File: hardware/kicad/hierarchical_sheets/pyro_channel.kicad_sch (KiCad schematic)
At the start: 22 parts, among them J2 282834-2, J3 282834-4, U2 ZXCT1110W5-7, U3 SI9926CDY

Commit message: test
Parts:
- C3: value DNP -> 100n
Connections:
- net VBAT: now also J2.2 (Pin_2); no longer J2.1 (Pin_1)
- net at R1.1, R3.1, U2.4 (Vs+): now also J2.1 (Pin_1); no longer J2.2 (Pin_2)
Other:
- moved on the sheet: J2
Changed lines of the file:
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@@
     )
   )
-  (symbol (lib_id "Connector:Screw_Terminal_01x02") (at 37.465 82.55 90) (unit 1)
+  (symbol (lib_id "Connector:Screw_Terminal_01x02") (at 40.005 82.55 270) (mirror x) (unit 1)
     (in_bom yes) (on_board yes) (dnp no)
-    (property "Reference" "J2" (at 29.845 77.47 90)
+    (property "Reference" "J2" (at 43.18 77.47 90)
       (effects (font (size 1.27 1.27)) (justify right))
     )
-    (property "Value" "282834-2" (at 29.845 79.375 90)
+    (property "Value" "282834-2" (at 43.18 79.375 90)
       (effects (font (size 1.27 1.27)) (justify right))
     )
-    (property "Footprint" "TerminalBlock_TE-Connectivity:TerminalBlock_TE_282834-2_1x02_P2.54mm_Horizontal" (at 37.465 82.55 0)
+    (property "Footprint" "TerminalBlock_TE-Connectivity:TerminalBlock_TE_282834-2_1x02_P2.54mm_Horizontal" (at 40.005 82.55 0)
       (effects (font (size 1.27 1.27)) hide)
     )
-    (property "Datasheet" "https://www.te.com/usa-en/product-282834-2.datasheet.pdf" (at 37.465 82.55 0)
+    (property "Datasheet" "https://www.te.com/usa-en/product-282834-2.datasheet.pdf" (at 40.005 82.55 0)
       (effects (font (size 1.27 1.27)) hide)
     )
-    (property "Digikey" "https://www.digikey.com/en/products/detail/te-connectivity-amp-connectors/282834-2/1150135" (at 37.465 82.55 90)
+    (property "Digikey" "https://www.digikey.com/en/products/detail/te-connectivity-amp-connectors/282834-2/1150135" (at 40.005 82.55 90)
       (effects (font (size 1.27 1.27)) hide)
     )
@@
       (effects (font (size 1.27 1.27)) (justify left))
     )
-    (property "Value" "DNP" (at 94.615 114.2937 0)
+    (property "Value" "100n" (at 94.615 114.2937 0)
       (effects (font (size 1.27 1.27)) (justify left))
     )

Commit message: power routing
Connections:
- net VBAT: now also J2.1 (Pin_1); no longer J2.2 (Pin_2)
- net VBAT_SWITCHED: now reaches R1.1, R3.1, U2.4 (Vs+)
- net VBAT_SWITCHED: now also J2.2 (Pin_2); no longer J2.1 (Pin_1)
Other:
- moved on the sheet: J2
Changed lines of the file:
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@@
     (effects (font (size 1 1)) (justify left bottom))
+  )
+  (label "VBAT_SWITCHED" (at 50.165 88.265 0) (fields_autoplaced)
+    (effects (font (size 1.27 1.27)) (justify left bottom))
   )
   (label "PYRO_SUPPLY_MONITORED." (at 114.3 88.265 180) (fields_autoplaced)
@@
     )
   )
-  (symbol (lib_id "Connector:Screw_Terminal_01x02") (at 40.005 82.55 270) (mirror x) (unit 1)
-    (in_bom yes) (on_board yes) (dnp no)
-    (property "Reference" "J2" (at 43.18 77.47 90)
+  (symbol (lib_id "Connector:Screw_Terminal_01x02") (at 37.465 82.55 90) (unit 1)
+    (in_bom yes) (on_board yes) (dnp no)
+    (property "Reference" "J2" (at 34.29 77.47 90)
       (effects (font (size 1.27 1.27)) (justify right))
     )
-    (property "Value" "282834-2" (at 43.18 79.375 90)
+    (property "Value" "282834-2" (at 34.29 79.375 90)
       (effects (font (size 1.27 1.27)) (justify right))
     )
-    (property "Footprint" "TerminalBlock_TE-Connectivity:TerminalBlock_TE_282834-2_1x02_P2.54mm_Horizontal" (at 40.005 82.55 0)
-      (effects (font (size 1.27 1.27)) hide)
-    )
-    (property "Datasheet" "https://www.te.com/usa-en/product-282834-2.datasheet.pdf" (at 40.005 82.55 0)
-      (effects (font (size 1.27 1.27)) hide)
-    )
-    (property "Digikey" "https://www.digikey.com/en/products/detail/te-connectivity-amp-connectors/282834-2/1150135" (at 40.005 82.55 90)
-      (effects (font (size 1.27 1.27)) hide)
-    )
+    (property "Footprint" "TerminalBlock_TE-Connectivity:TerminalBlock_TE_282834-2_1x02_P2.54mm_Horizontal" (at 37.465 82.55 0)
+      (effects (font (size 1.27 1.27)) hide)
+    )
+    (property "Datasheet" "https://www.te.com/usa-en/product-282834-2.datasheet.pdf" (at 37.465 82.55 0)
+      (effects (font (size 1.27 1.27)) hide)
+    )
+    (property "Digikey" "https://www.digikey.com/en/products/detail/te-connectivity-amp-connectors/282834-2/1150135" (at 37.465 82.55 90)
+      (effects (font (size 1.27 1.27)) hide)
+    )

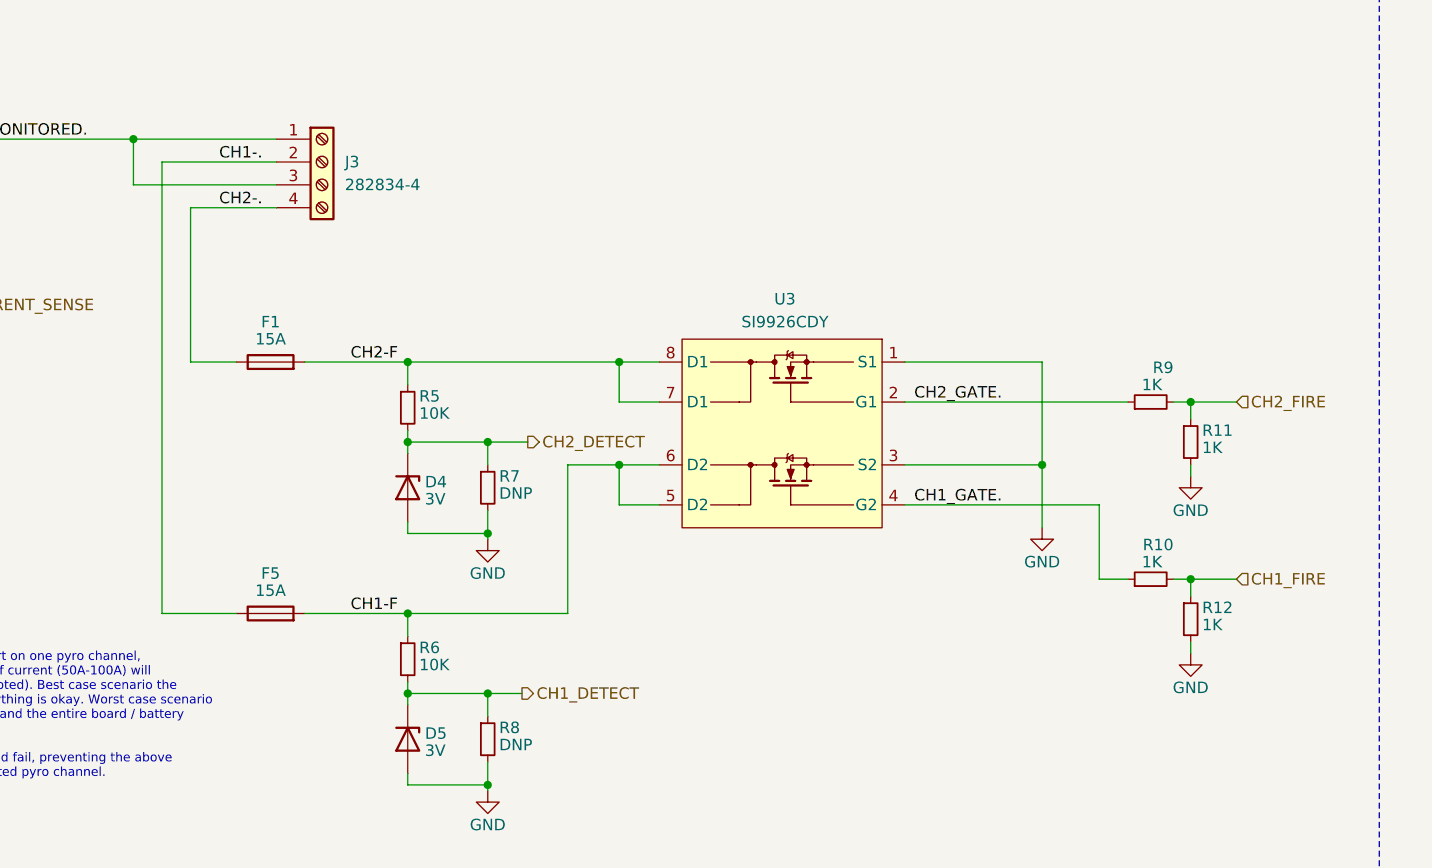
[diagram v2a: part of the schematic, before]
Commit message: redoing the beautiful traces
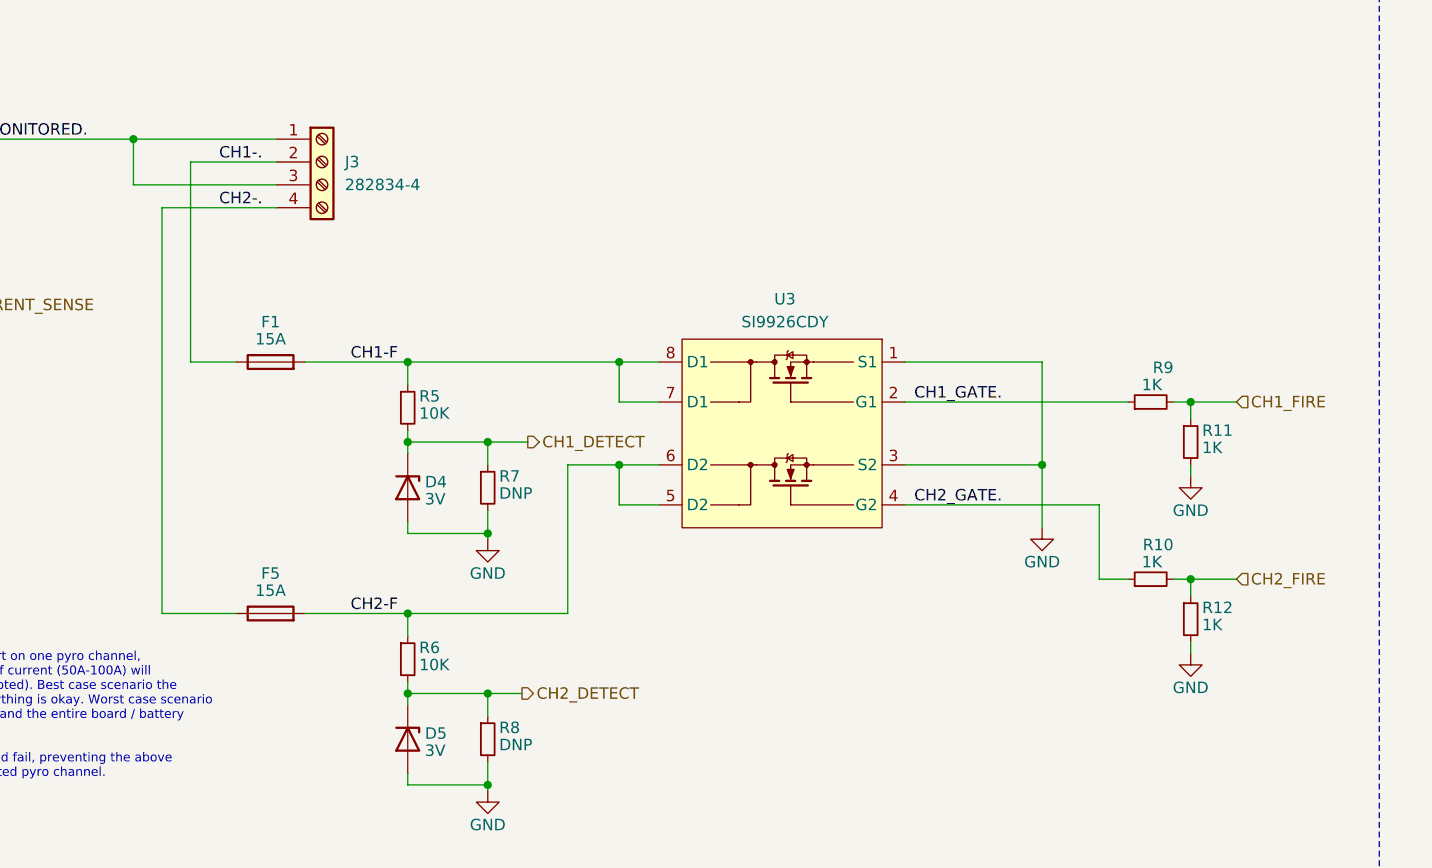
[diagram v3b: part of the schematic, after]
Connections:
- net CH1-.: now also F1.1; no longer F5.1
- net CH1-F: now also F1.2, R5.1, U3.7 (D1), U3.8 (D1); no longer F5.2, R6.1, U3.5 (D2), U3.6 (D2)
- net CH1_DETECT: now also D4.3 (K), R5.2, R7.1; no longer D5.3 (K), R6.2, R8.1
- net CH1_FIRE: now also R11.1, R9.2; no longer R10.2, R12.1
- net CH1_GATE.: now also R9.1, U3.2 (G1); no longer R10.1, U3.4 (G2)
- net CH2-.: now also F5.1; no longer F1.1
- net CH2-F: now also F5.2, R6.1, U3.5 (D2), U3.6 (D2); no longer F1.2, R5.1, U3.7 (D1), U3.8 (D1)
- net CH2_DETECT: now also D5.3 (K), R6.2, R8.1; no longer D4.3 (K), R5.2, R7.1
- net CH2_FIRE: now also R10.2, R12.1; no longer R11.1, R9.2
- net CH2_GATE.: now also R10.1, U3.4 (G2); no longer R9.1, U3.2 (G1)
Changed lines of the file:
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@@
+    (stroke (width 0) (type default))
+  )
+  (wire (pts (xy 125.73 90.805) (xy 125.73 113.03))
     (stroke (width 0) (type default))
   )
@@
     (stroke (width 0) (type default))
   )
-  (wire (pts (xy 122.555 90.805) (xy 122.555 140.97))
-    (stroke (width 0) (type default))
-  )
   (wire (pts (xy 236.855 124.46) (xy 236.855 125.73))
     (stroke (width 0) (type default))
   )
-  (wire (pts (xy 125.73 95.885) (xy 125.73 113.03))
-    (stroke (width 0) (type default))
-  )
-  (wire (pts (xy 125.73 95.885) (xy 135.255 95.885))
-    (stroke (width 0) (type default))
-  )
   (wire (pts (xy 37.465 88.265) (xy 37.465 87.63))
     (stroke (width 0) (type default))
@@
     (stroke (width 0) (type default))
   )
+  (wire (pts (xy 122.555 140.97) (xy 122.555 95.885))
+    (stroke (width 0) (type default))
+  )
   (wire (pts (xy 81.915 119.38) (xy 92.71 119.38))
     (stroke (width 0) (type default))
@@
   )
   (wire (pts (xy 149.86 148.59) (xy 149.86 149.86))
+    (stroke (width 0) (type default))
+  )
+  (wire (pts (xy 125.73 90.805) (xy 135.255 90.805))
     (stroke (width 0) (type default))
   )
@@
     (stroke (width 0) (type default))
   )
+  (wire (pts (xy 122.555 95.885) (xy 135.255 95.885))
+    (stroke (width 0) (type default))
+  )
   (polyline (pts (xy 257.81 72.39) (xy 257.81 169.545))
     (stroke (width 0) (type dash))
   )
   (wire (pts (xy 158.75 160.02) (xy 158.75 160.655))
-    (stroke (width 0) (type default))
-  )
-  (wire (pts (xy 122.555 90.805) (xy 135.255 90.805))
     (stroke (width 0) (type default))
   )
@@
     (effects (font (size 1.27 1.27)) (justify right bottom))
   )
+  (label "CH1-." (at 128.905 90.805 0) (fields_autoplaced)
+    (effects (font (size 1.27 1.27)) (justify left bottom))
+  )
+  (label "CH2-F" (at 143.51 140.97 0) (fields_autoplaced)
+    (effects (font (size 1.27 1.27)) (justify left bottom))
+  )
+  (label "CH2_GATE." (at 215.9 128.905 180) (fields_autoplaced)
+    (effects (font (size 1.27 1.27)) (justify right bottom))
+  )
+  (label "CH1_GATE." (at 215.9 117.475 180) (fields_autoplaced)
+    (effects (font (size 1.27 1.27)) (justify right bottom))
+  )
   (label "CH2-." (at 128.905 95.885 0) (fields_autoplaced)
     (effects (font (size 1.27 1.27)) (justify left bottom))
   )
-  (label "CH1-F" (at 143.51 140.97 0) (fields_autoplaced)
-    (effects (font (size 1.27 1.27)) (justify left bottom))
-  )
-  (label "CH1_GATE." (at 215.9 128.905 180) (fields_autoplaced)
-    (effects (font (size 1.27 1.27)) (justify right bottom))
-  )
-  (label "CH2_GATE." (at 215.9 117.475 180) (fields_autoplaced)
-    (effects (font (size 1.27 1.27)) (justify right bottom))
-  )
-  (label "CH1-." (at 128.905 90.805 0) (fields_autoplaced)
-    (effects (font (size 1.27 1.27)) (justify left bottom))
-  )
-  (label "CH2-F" (at 143.51 113.03 0) (fields_autoplaced)
+  (label "CH1-F" (at 143.51 113.03 0) (fields_autoplaced)
     (effects (font (size 1.27 1.27)) (justify left bottom))
   )
@@
     (effects (font (size 1.27 1.27)) (justify left))
   )
-  (hierarchical_label "CH2_DETECT" (shape output) (at 163.195 121.92 0) (fields_autoplaced)
-    (effects (font (size 1.27 1.27)) (justify left))
-  )
-  (hierarchical_label "CH1_FIRE" (shape input) (at 241.935 137.16 0) (fields_autoplaced)
+  (hierarchical_label "CH2_DETECT" (shape output) (at 162.56 149.86 0) (fields_autoplaced)
+    (effects (font (size 1.27 1.27)) (justify left))
+  )
+  (hierarchical_label "CH1_FIRE" (shape input) (at 241.935 117.475 0) (fields_autoplaced)
     (effects (font (size 1.27 1.27)) (justify left))
   )
@@
     (effects (font (size 1.27 1.27)) (justify right))
   )
-  (hierarchical_label "CH1_DETECT" (shape output) (at 162.56 149.86 0) (fields_autoplaced)
-    (effects (font (size 1.27 1.27)) (justify left))
-  )
-  (hierarchical_label "CH2_FIRE" (shape input) (at 241.935 117.475 0) (fields_autoplaced)
-    (effects (font (size 1.27 1.27)) (justify left))
-  )
+  (hierarchical_label "CH1_DETECT" (shape output) (at 163.195 121.92 0) (fields_autoplaced)
+    (effects (font (size 1.27 1.27)) (justify left))
+  )
+  (hierarchical_label "CH2_FIRE" (shape input) (at 241.935 137.16 0) (fields_autoplaced)
+    (effects (font (size 1.27 1.27)) (justify left))
+  )

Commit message: appended .off to old files
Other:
- note removed: "REDO CALCULATION"
